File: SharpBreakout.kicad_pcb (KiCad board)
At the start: 4 copper layers, 36.8 x 30.5 mm, 14 parts, among them J1 Conn_01x21_MountingPin, J2 Conn_01x02_Pin, J3 Conn_02x10_Odd_Even, J4 Conn_02x02_Odd_Even, J5 Conn_02x10_Odd_Even, J6 Conn_01x02_Pin, U1 SiP32431DR3, U2 SiP32431DR3

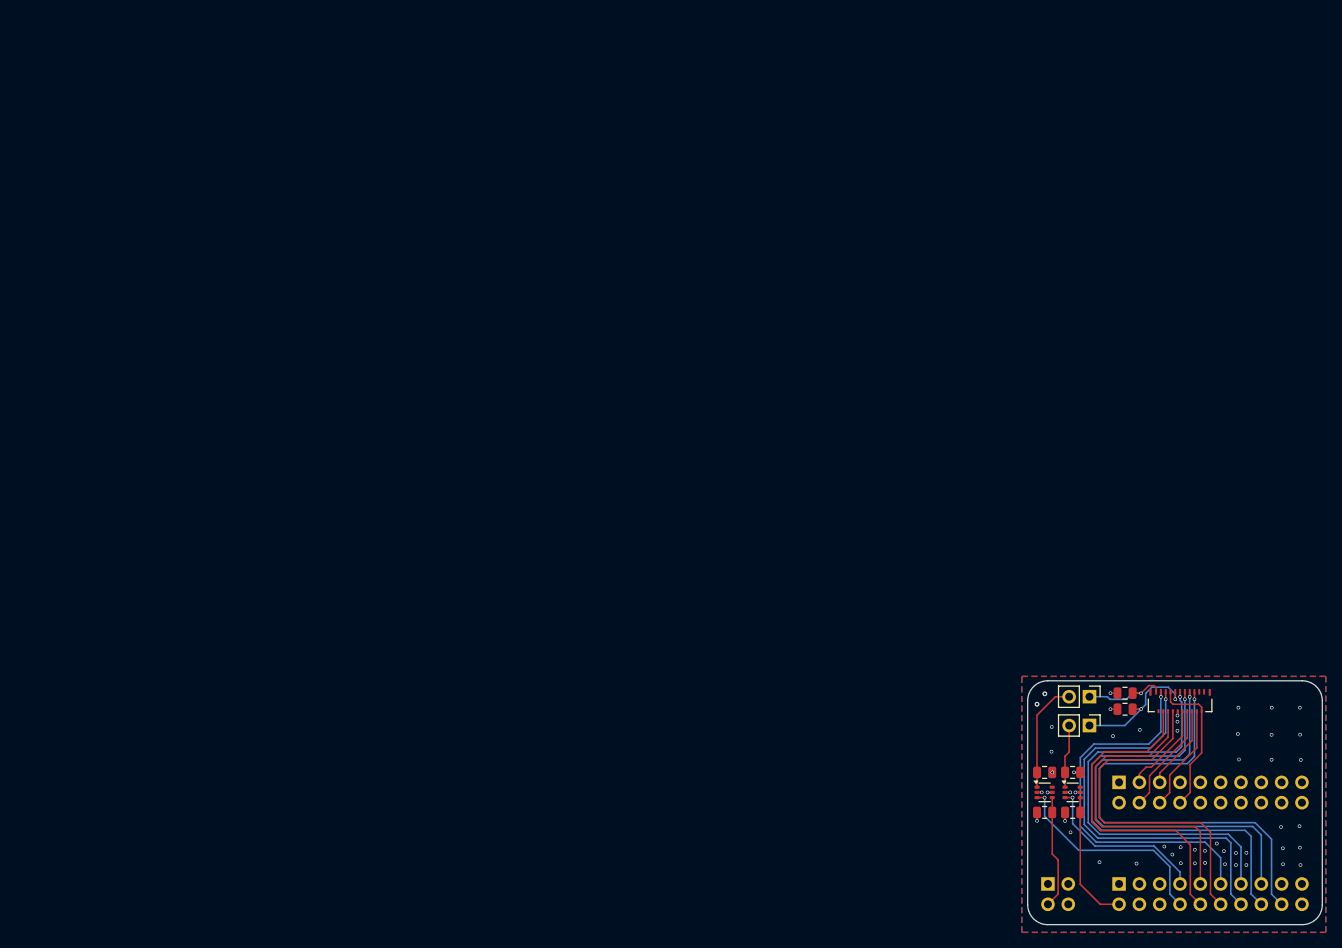
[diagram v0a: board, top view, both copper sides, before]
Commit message: Updated pinout for better performance, all colors on one GPIO periphral, all horizontal controls on same GPIO peripheral, all vertical controls on same GPIO peripheral
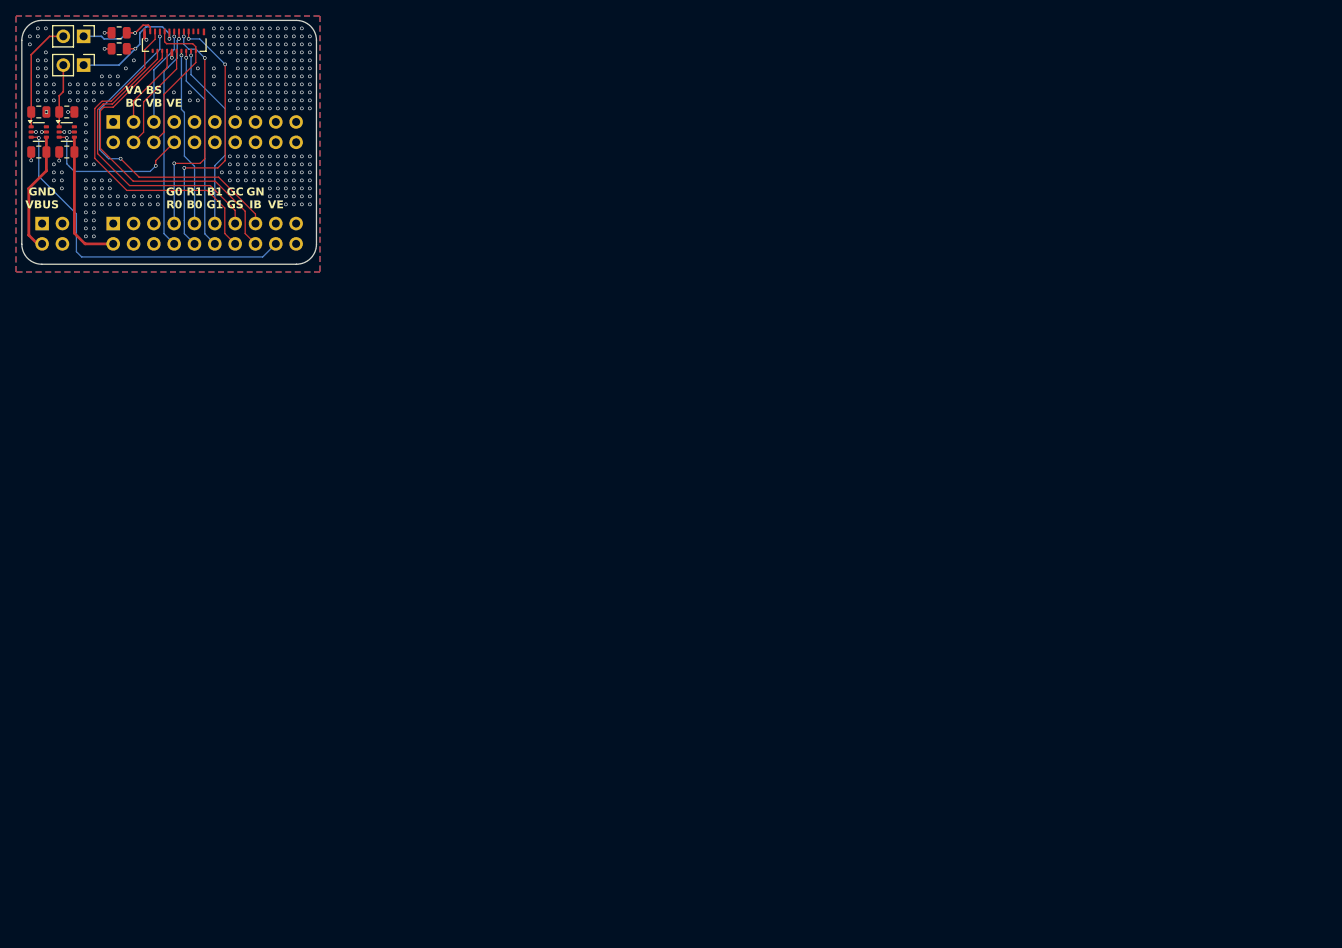
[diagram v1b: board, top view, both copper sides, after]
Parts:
- J1: value Conn_01x21_MountingPin -> Molex 503566-2102
- U1, U2: value SiP32431DR3 -> SiP32432DR3
- moved J2 150.4 mm to (7.72, 1.99)
- moved J3 150.4 mm to (11.4, 12.7)
- moved J6 150.4 mm to (7.72, 5.59)
- moved C1 150.4 mm to (12.2, 1.55)
- moved C2 150.4 mm to (12.2, 3.55)
- moved C3 150.4 mm to (2.12, 16.4)
- moved C4 150.4 mm to (2.12, 11.4)
- moved C5 150.4 mm to (5.62, 16.4)
- moved C6 150.4 mm to (5.62, 11.4)
- moved J1 150.4 mm to (19.1, 2.54)
- moved J4 150.4 mm to (2.54, 25.4)
- moved J5 150.4 mm to (11.4, 25.4)
- moved U1 150.4 mm to (2.12, 13.9)
- moved U2 150.4 mm to (5.62, 13.9)
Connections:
- J3 pad 3: /BCK -> /VA
- J3 pad 4: /R1 -> /BCK
- J3 pad 5: /G1 -> /BSP
- J3 pad 6: /B1 -> /VB
- J3 pad 8: /VB -> /VDDIO_EN
- J5 pad 10: /GCK -> /B0
- J5 pad 11: /GSP -> /B1
- J5 pad 12: /VA -> /G1
- J5 pad 13: /BSP -> /GCK
- J5 pad 14: /GEN -> /GSP
- J5 pad 15: /G0 -> /GEN
- J5 pad 16: /R0 -> /INTB
- J5 pad 18: /B0 -> /VBUS_EN
- J5 pad 7: /VDDIO_EN -> /G0
- J5 pad 8: /VBUS_EN -> /R0
- J5 pad 9: /INTB -> /R1
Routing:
- net /BSP: track 52.0 -> 12.4 mm
- net /VA: track 44.4 -> 10.6 mm
- net /R0: track 56.4 -> 27.9 mm
- net /G0: track 54.3 -> 29.1 mm, vias 1 -> 3
- net /B0: track 58.0 -> 34.4 mm, vias 1 -> 3
- net /VBUS_EN: track 26.8 -> 43.0 mm
- net /G1: track 10.6 -> 25.6 mm, vias 0 -> 1
- net /B1: track 13.4 -> 23.9 mm, vias 0 -> 1
- net /GEN: track 52.3 -> 41.9 mm, vias 1 -> 2
- net /R1: track 13.9 -> 22.3 mm, vias 0 -> 1
- net /GSP: track 47.4 -> 43.5 mm, vias 1 -> 0
- net /GCK: track 42.1 -> 38.4 mm
- net /BCK: track 11.5 -> 13.7 mm
- net /VDDIO_EN: track 21.6 -> 19.9 mm, vias 1 -> 2
- net GND: track 8.67 -> 10.1 mm, vias 52 -> 298
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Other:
- board text added: "B1 G1"
- board text added: "BS VB"
- board text added: "G0 R0"
- board text added: "GC GS"
- board text added: "GN IB"
- board text added: "GND VBUS"
- board text added: "R1 B0"
- board text added: "VA BC"
- board text added: "VE"
